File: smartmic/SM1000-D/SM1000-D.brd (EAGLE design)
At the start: 65 x 100 mm, 199 parts, among them CN1 HDR100-3, CN10 ST-3509, CN11 HDR100-3, CN12 HRS-A3C-16DA, CN2 JS-MU3-002, CN3 DS-0518, CN4 RJ-45, CN5 ST-3509, CN6 ST-3509, CN7 ST-3509, CN8 ST-3509, CN9 ST-3509, J1 JMP-2PIN, J3 JMP-2PIN, J4 JMP-2PIN, P1 TPAD50, P10 TPAD50, P11 TPAD50, P12 TPAD50, P13 TPAD50, P14 TPAD50, P16 TPAD50, P18 TPAD50, P19 TPAD50, P2 TPAD50, P20 TPAD50, P3 TPAD50, P4 TPAD50, P5 TPAD50, P6 TPAD50, P7 TPAD50, P8 TPAD50, P9 TPAD50, SW1 TS-026, SW2 TS-026, SW3 DPDT, SW4 TS-026, SW5 TS-02B, T1 SM-LP-5001, T2 SM-LP-5001, U1 STM32F407, U2 LD3985M33R, U3 STMPS2141, U4 EMIF02-USB03F2, U5 TPS54329E, U6 LMV341, U7 LMV341, U8 LM386M-1, U9 LMV341

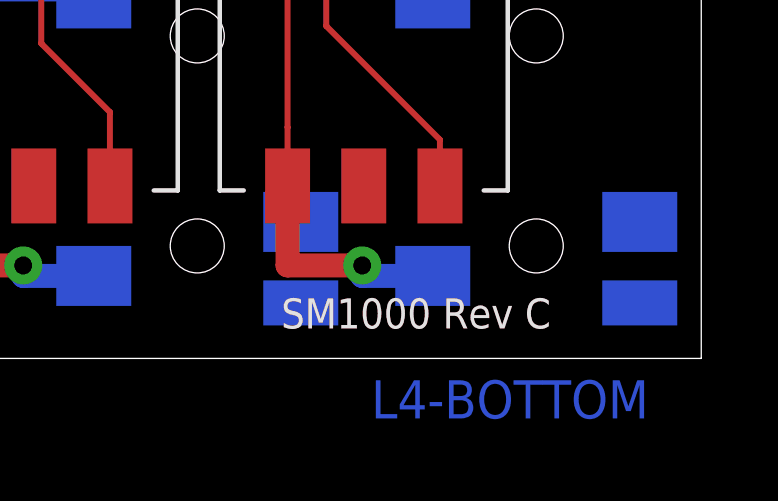
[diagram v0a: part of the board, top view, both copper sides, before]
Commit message: Complete SM1000-C -> SM1000-D update RGB
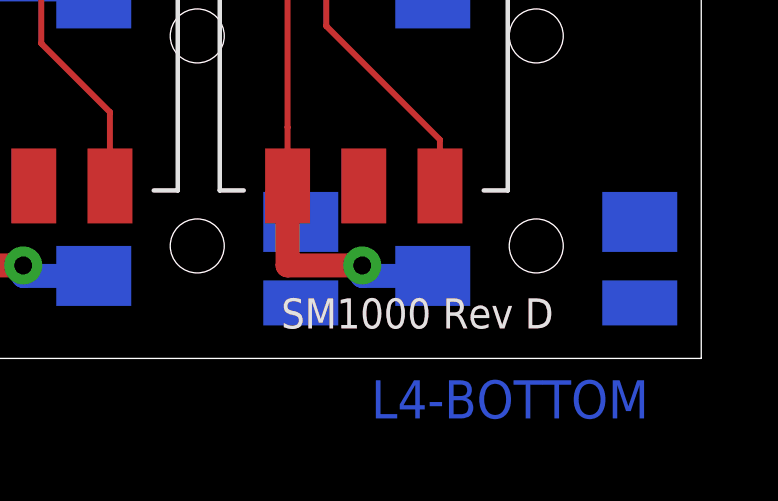
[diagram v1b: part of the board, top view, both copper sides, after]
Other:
- board text added: "DRL-TBL-SM1000-D.PDF"
- board text added: "SM1000 Rev D"
- board text removed: "DRL-TBL-SM1000-C.PDF"
- board text removed: "SM1000 Rev C"
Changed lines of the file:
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@@
 <grid distance="0.5" unitdist="mm" unit="mm" style="dots" multiple="1" display="yes" altdistance="0.1" altunitdist="mm" altunit="mm"/>
 <layers>
-<layer number="1" name="Top" color="4" fill="1" visible="no" active="yes"/>
+<layer number="1" name="Top" color="4" fill="1" visible="yes" active="yes"/>
 <layer number="2" name="GND" color="3" fill="1" visible="no" active="yes"/>
 <layer number="3" name="Route3" color="4" fill="3" visible="no" active="no"/>
@@
 <layer number="14" name="Route14" color="1" fill="6" visible="no" active="no"/>
 <layer number="15" name="VDD" color="6" fill="1" visible="no" active="yes"/>
-<layer number="16" name="Bottom" color="1" fill="1" visible="yes" active="yes"/>
-<layer number="17" name="Pads" color="2" fill="1" visible="no" active="yes"/>
-<layer number="18" name="Vias" color="2" fill="1" visible="no" active="yes"/>
-<layer number="19" name="Unrouted" color="6" fill="1" visible="no" active="yes"/>
+<layer number="16" name="Bottom" color="1" fill="1" visible="no" active="yes"/>
+<layer number="17" name="Pads" color="2" fill="1" visible="yes" active="yes"/>
+<layer number="18" name="Vias" color="2" fill="1" visible="yes" active="yes"/>
+<layer number="19" name="Unrouted" color="6" fill="1" visible="yes" active="yes"/>
 <layer number="20" name="Dimension" color="15" fill="1" visible="yes" active="yes"/>
-<layer number="21" name="tPlace" color="7" fill="1" visible="no" active="yes"/>
-<layer number="22" name="bPlace" color="7" fill="1" visible="yes" active="yes"/>
-<layer number="23" name="tOrigins" color="15" fill="1" visible="no" active="yes"/>
-<layer number="24" name="bOrigins" color="15" fill="1" visible="yes" active="yes"/>
-<layer number="25" name="tNames" color="7" fill="1" visible="no" active="yes"/>
-<layer number="26" name="bNames" color="7" fill="1" visible="yes" active="yes"/>
+<layer number="21" name="tPlace" color="7" fill="1" visible="yes" active="yes"/>
+<layer number="22" name="bPlace" color="7" fill="1" visible="no" active="yes"/>
+<layer number="23" name="tOrigins" color="15" fill="1" visible="yes" active="yes"/>
+<layer number="24" name="bOrigins" color="15" fill="1" visible="no" active="yes"/>
+<layer number="25" name="tNames" color="7" fill="1" visible="yes" active="yes"/>
+<layer number="26" name="bNames" color="7" fill="1" visible="no" active="yes"/>
 <layer number="27" name="tValues" color="7" fill="1" visible="no" active="yes"/>
 <layer number="28" name="bValues" color="7" fill="1" visible="no" active="yes"/>
@@
 <wire x1="59.5" y1="32.5" x2="20.5" y2="32.5" width="0.1" layer="22"/>
 <wire x1="20.5" y1="32.5" x2="20.5" y2="26.5" width="0.1" layer="22"/>
-<text x="51" y="1" size="1" layer="1" font="vector" ratio="15">SM1000 Rev C</text>
-<text x="51" y="1" size="1" layer="21" font="vector" ratio="15">SM1000 Rev C</text>
+<text x="51" y="1" size="1" layer="1" font="vector" ratio="15">SM1000 Rev D</text>
+<text x="51" y="1" size="1" layer="21" font="vector" ratio="15">SM1000 Rev D</text>
 <wire x1="43.4746" y1="53.8382" x2="43.4746" y2="52.111" width="0.1016" layer="144"/>
 <wire x1="42.611" y1="52.9746" x2="44.3382" y2="52.9746" width="0.1016" layer="144"/>
@@
 <wire x1="11.111" y1="95.686" x2="12.8382" y2="95.686" width="0.1016" layer="144"/>
 <wire x1="12.8382" y1="95.686" x2="11.111" y2="97.4132" width="0.1016" layer="144"/>
-<text x="1" y="-5" size="1.27" layer="144" ratio="10">DRL-TBL-SM1000-C.PDF</text>
+<text x="1" y="-5" size="1.27" layer="144" ratio="10">DRL-TBL-SM1000-D.PDF</text>
 </plain>
 <attributes>

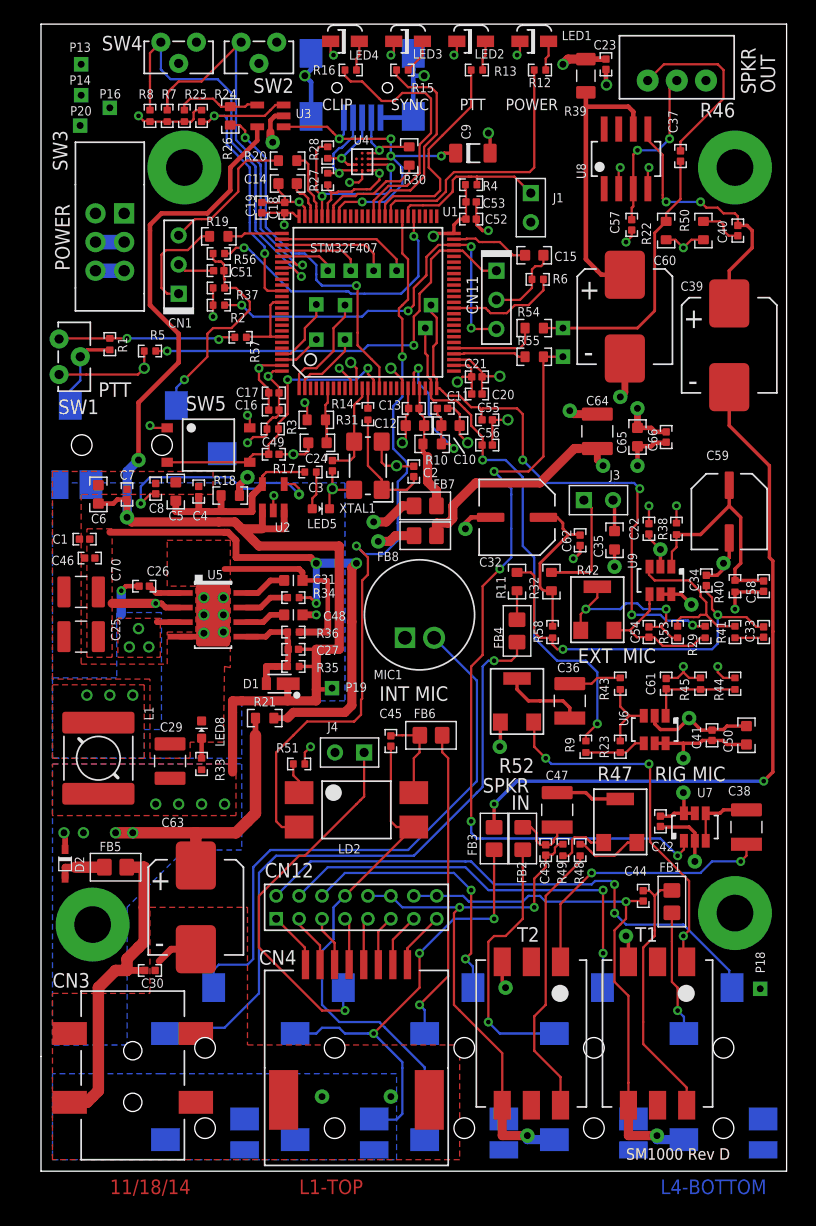
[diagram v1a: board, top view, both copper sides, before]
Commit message: Changed USB con  position, Changed SW 1,2,4 footprint CHanged MIC footprint
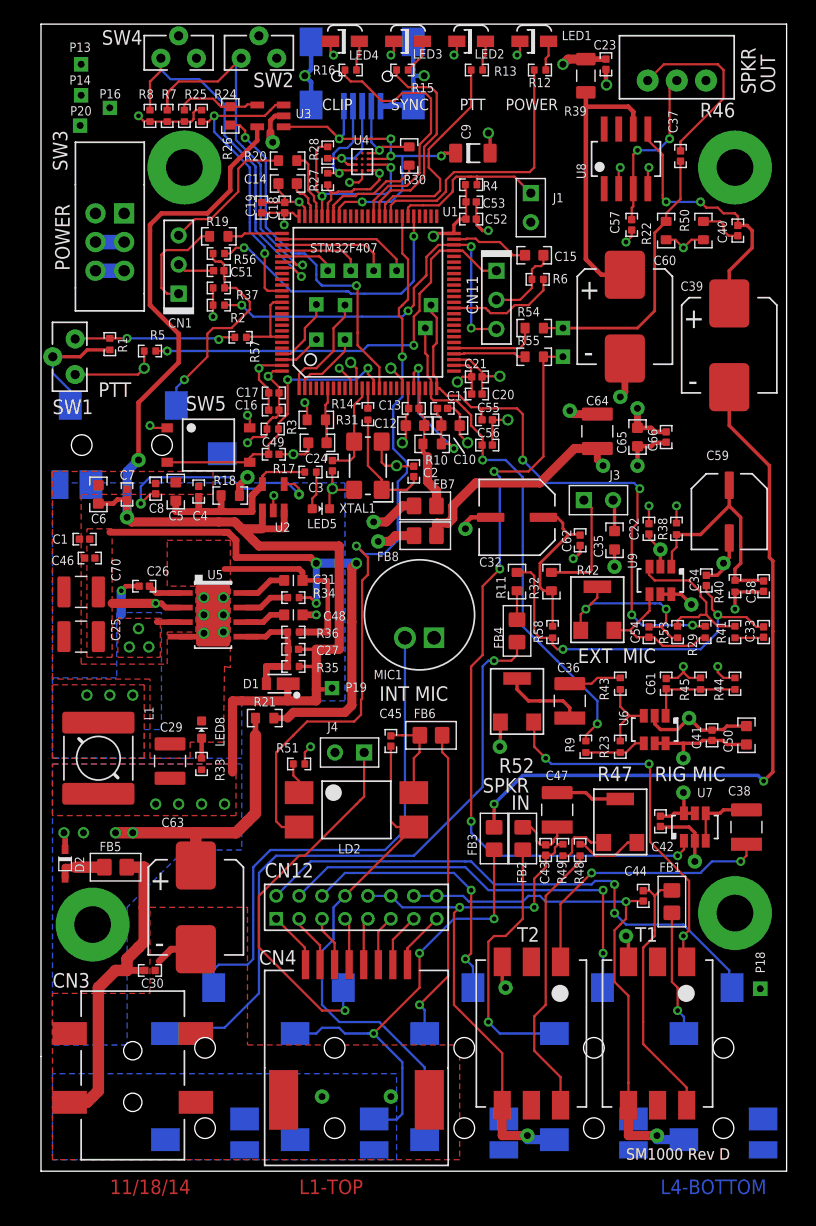
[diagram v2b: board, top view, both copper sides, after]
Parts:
- moved CN2 1.00 mm to (28.0, 95.7)
- moved SW1 0.50 mm to (2.00, 71.0)
- moved SW2 0.50 mm to (19.0, 98.0)
- moved SW4 0.50 mm to (12.0, 98.0)
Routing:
- net N$60: track 50.1 -> 44.8 mm
- net !BACK!: track 36.2 -> 32.5 mm
- net GND: track 200.8 -> 203.5 mm
- net !SELECT!: track 36.2 -> 34.2 mm
- net N$22: track 7.02 -> 8.67 mm
- net N$14: track 15.5 -> 14.1 mm
- net VDD: track 62.7 -> 61.3 mm
- net N$23: track 8.91 -> 10.2 mm
- net N$28: track 6.97 -> 7.97 mm
- net VBUS: track 31.2 -> 32.0 mm
- net DAC1_OUT: track 69.2 -> 68.3 mm
- net AIN1: track 46.5 -> 45.7 mm
- net N$25: track 33.6 -> 33.0 mm
- net OTG_OVR_CUR: track 26.8 -> 26.3 mm

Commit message: Incorporated new PTT SW & TrimPOTs
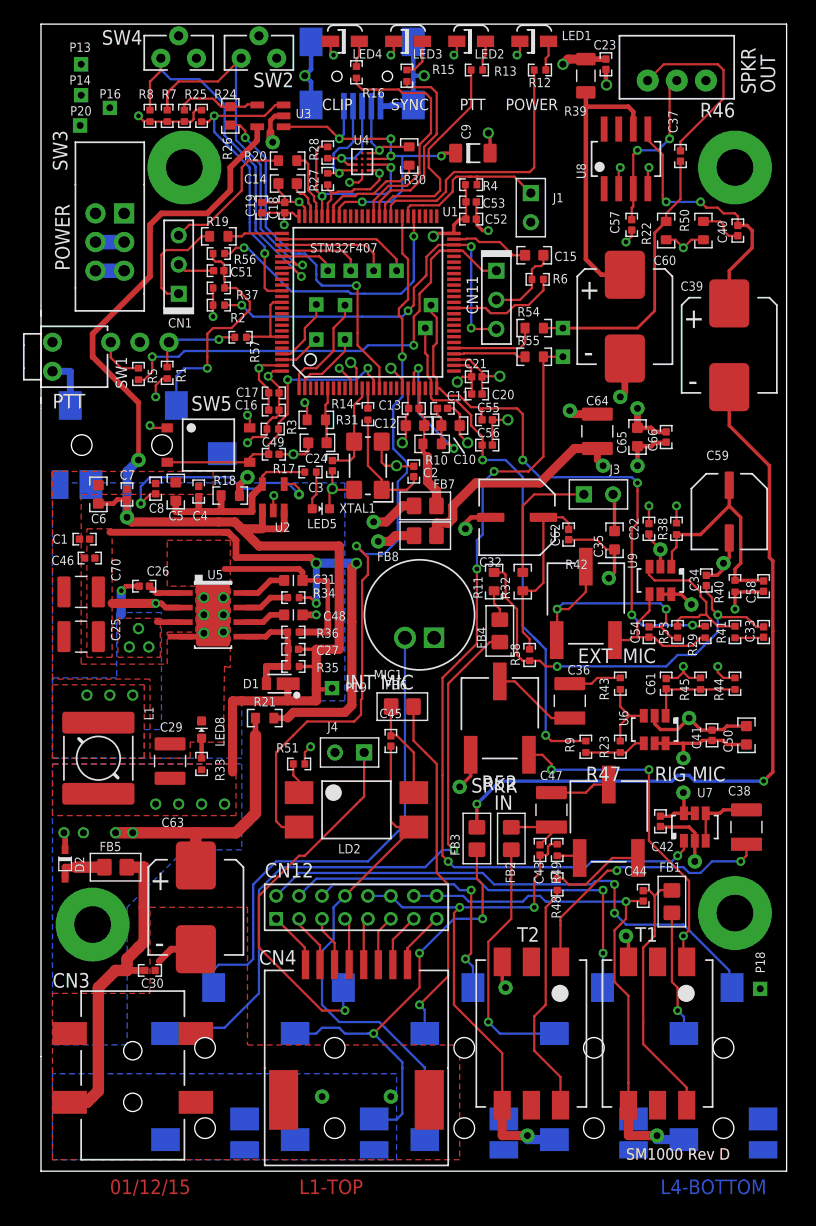
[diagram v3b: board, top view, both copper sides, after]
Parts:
- R42, R47, R52: device _RoweTel:PAN-EVM1D -> _RoweTel:POT3361
- SW1: value TS-026 -> SW-SPDT-8US8WR2C2M7RES; device _RoweTel:TS-026 -> _RoweTel:SW-SPDT-8US8WR2C2M7RES
- moved R1 5.59 mm to (11.0, 69.6)
- moved R48 3.61 mm to (45.0, 25.0)
- moved FB6 3.54 mm to (31.5, 40.5)
- moved R58 2.83 mm to (42.6, 45.0)
- moved R32 2.50 mm to (42.0, 51.4)
- moved R5 2.24 mm to (8.50, 69.5), turned to 270 degrees
- moved R52 2.12 mm to (40.0, 39.5)
- moved R11 2.00 mm to (39.5, 51.4)
- moved FB3 1.50 mm to (38.0, 29.0)
- moved FB4 1.50 mm to (40.0, 47.1)
- moved C62 1.12 mm to (46.0, 55.5)
- moved R42 1.12 mm to (47.5, 49.5)
- moved FB2 1.00 mm to (41.0, 29.0)
- moved R47 1.00 mm to (49.5, 30.5)
- moved SW1 1.00 mm to (1.00, 71.0), turned to 0 degrees
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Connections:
- net GND: now also SW1.G1, SW1.G2; no longer SW1.3
- net N$14: now also SW1.4; no longer SW1.2
- net VDD: now also SW1.6; no longer SW1.1
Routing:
- net N$41: track 16.4 -> 22.6 mm
- net N$14: track 14.1 -> 8.15 mm, vias 2 -> 1
- net DAC1_OUT: track 68.3 -> 73.5 mm
- net N$78: track 24.4 -> 20.5 mm
- net VDD: track 61.3 -> 57.7 mm, vias 15 -> 14
- net N$73: track 27.4 -> 31.0 mm
- net N$25: track 33.0 -> 36.6 mm
- net USART3_TX: track 37.6 -> 40.9 mm
- net N$61: track 5.04 -> 2.04 mm
- net N$81: track 67.9 -> 65.6 mm
- net N$82: track 5.89 -> 8.20 mm
- net N$45: track 14.1 -> 16.1 mm
- net N$63: track 31.8 -> 29.8 mm
- net LED-ERR: track 22.7 -> 20.8 mm
- net GND: track 203.5 -> 205.3 mm
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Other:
- board text added: "01/12/15"
- board text added: "L3-VDD-AVDD"
- board text removed: "11/18/14"
- board text removed: "L3-VDD\AVDD"
